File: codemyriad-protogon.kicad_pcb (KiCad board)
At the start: 2 copper layers, 54.3 x 36.6 mm, 14 parts, among them J1 Hexpansion-Connector, J2 Conn_02x10_Odd_Even, P1 PZ254V-11-02P, U1 ZD24C64A-XGMT, U2 SM04B-SRSS-TB_(LF)(SN)

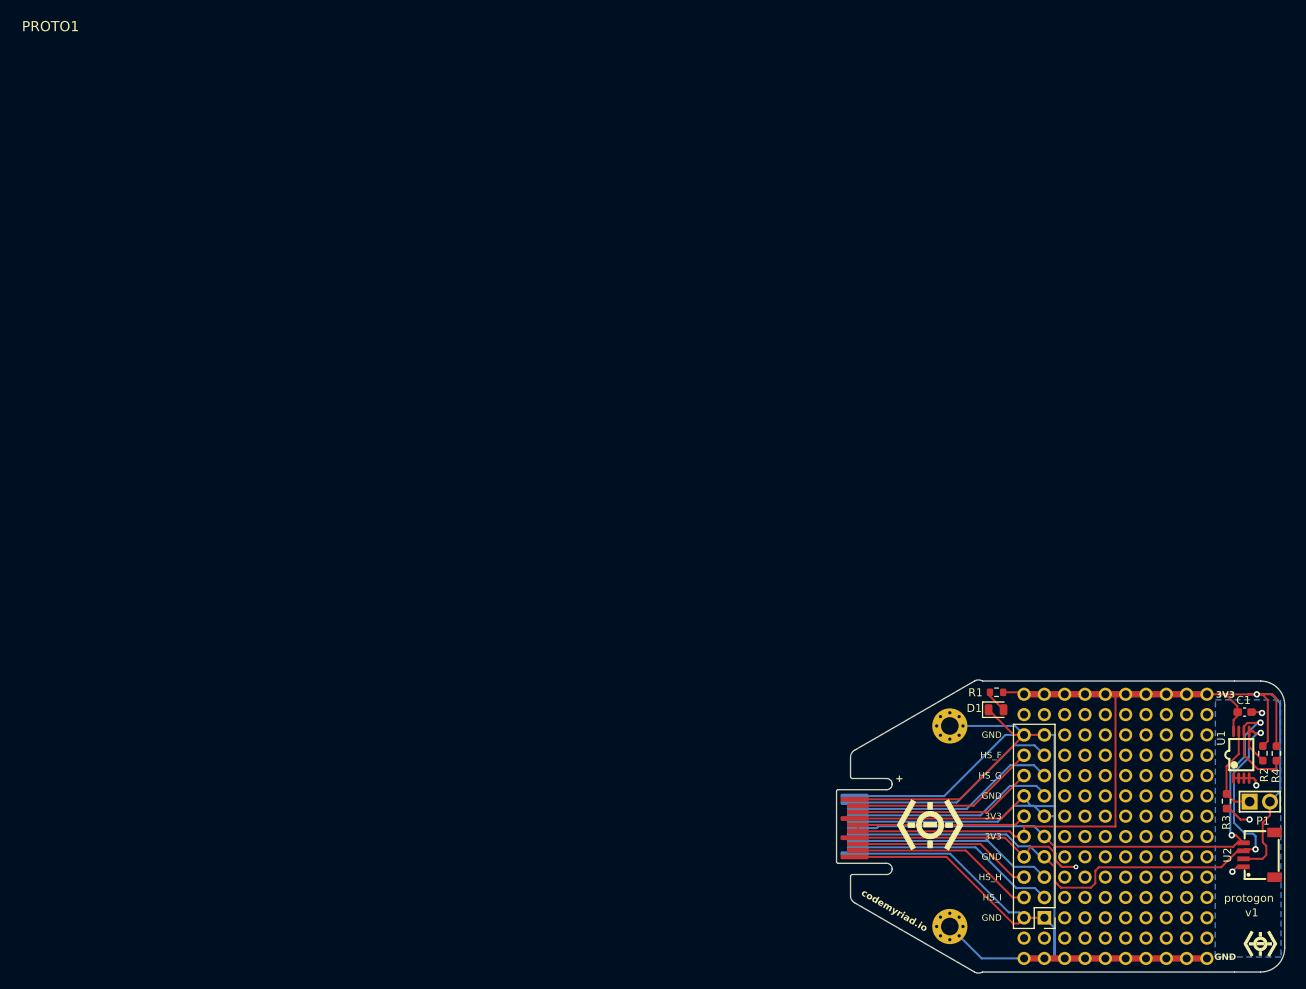
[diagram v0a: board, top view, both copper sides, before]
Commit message: Silkscreen cleanup, green soldermask; regenerate production files
Silkscreen:
- Remove the stray '+' near the edge connector and the 'v1' under 'protogon'
- Add 'WP' above the P1 write-protect jumper and 'qwiic' under U2
- Center the small hex logo (both faces) between the hole grid and board edge
- Hide the PROTO1 reference that plotted at the origin, far off-board

Soldermask changes from black to standard green (#0E6B2E in the stackup
so renders look like a real light-green board; the gbrjob says 'Green').

All fabrication outputs regenerated and validated against the prototype
gerbers: copper, masks, edge cuts, drills and positions are byte-identical;
only the silkscreen layers and gbrjob metadata changed. DRC/ERC clean.
Renders refreshed (the committed ones were stale, generated before the
text rotation).

Co-Authored-By: Claude Fable 5 <noreply@anthropic.com>
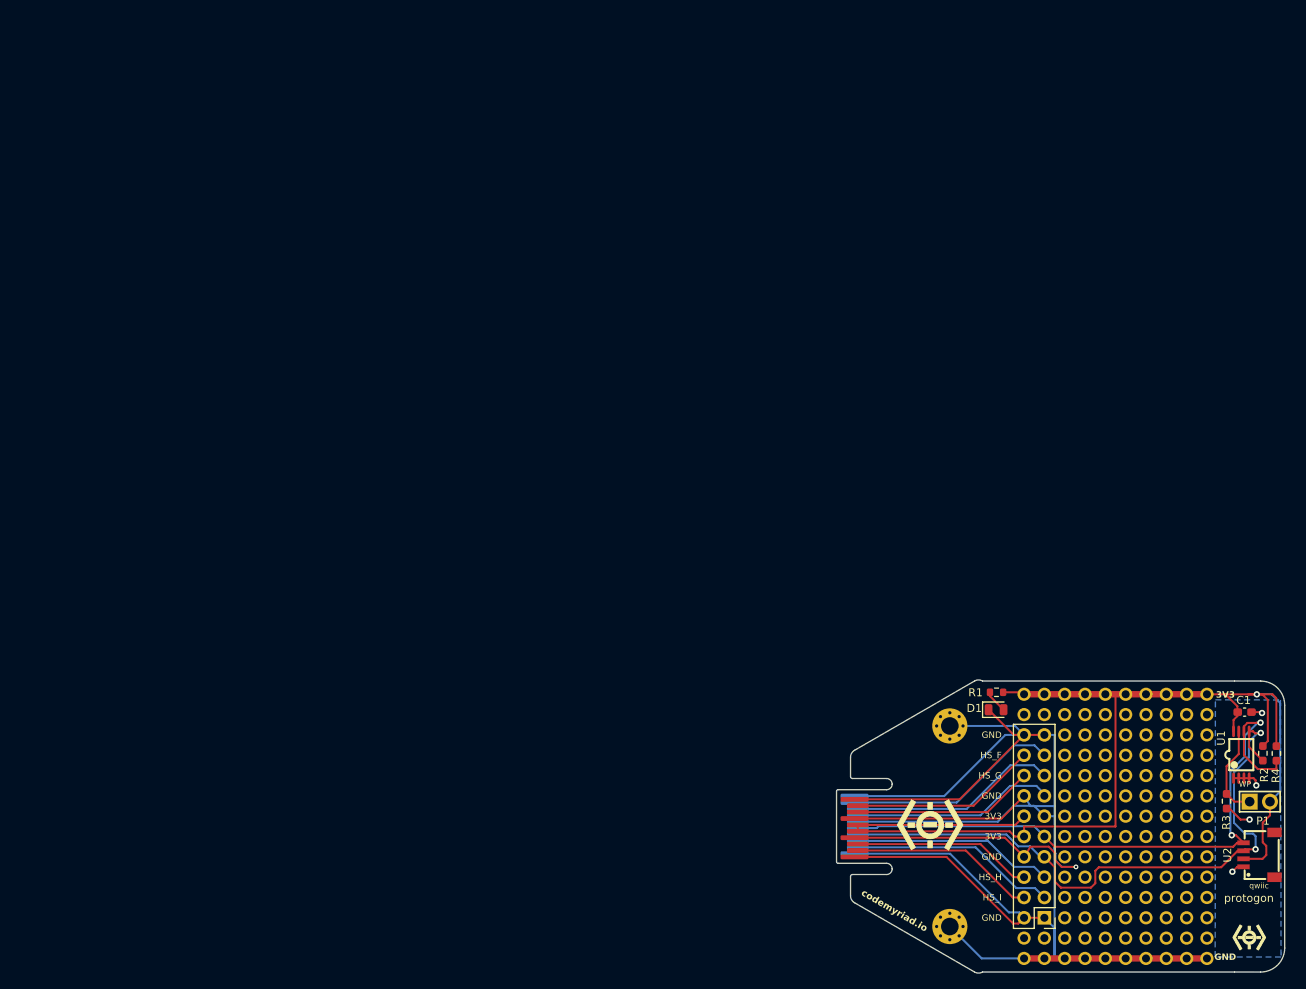
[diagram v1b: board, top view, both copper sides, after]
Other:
- board text added: "FAB: 1.0mm FR4, green soldermask, ENIG finish, no bevel on edge connector tab"
- board text added: "WP"
- board text added: "qwiic"
- board text removed: "+"
- board text removed: "FAB: 1.0mm FR4, black soldermask, ENIG finish, no bevel on edge connector tab"
- board text removed: "v1"
